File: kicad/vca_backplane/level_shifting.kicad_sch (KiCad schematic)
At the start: 8 parts, among them Q3 BSS138, Q4 BSS138, U2 74HCT245, U3 74LVC245

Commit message: v0.2 of backplane submitted to jlcpcb
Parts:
- added R24, R26, R27, R28, R29: 10k, Resistor_SMD:R_0603_1608Metric, symbol Device:R
- C2, C3: LCSC (none) -> C14663; LCSC Part C14663 -> (none)
- Q3, Q4: LCSC (none) -> C82045; LCSC Part C82045 -> (none)
- R1, R2: LCSC (none) -> C22978; LCSC Part C22978 -> (none)
- U2: LCSC (none) -> C5980; LCSC Part C5980 -> (none)
- U3: LCSC (none) -> C6082; LCSC Part C6082 -> (none)
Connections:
- net GND: now also R24.1, R26.1, R27.2, R28.1, R29.1
- net SPI_CLK_3V: now also U2.4 (A2)
- net SPI_MOSI_3V: now also U2.5 (A3)
- net SPI_MOSI2_5V: now reaches U2.15 (B3)
- net SPI_CLK2_5V: now reaches U2.16 (B2)
- net at U2.6 (A4): now also R24.2
- net at U2.7 (A5): now also R26.2
- net at U2.8 (A6): now also R29.2
- net at U2.9 (A7): now also R28.2
- net at U3.2 (A0): now also R27.1
- net SPI_CLK_5V renamed SPI_CLK1_5V
- net SPI_MOSI_5V renamed SPI_MOSI1_5V
- no-connect marks 14 -> 5
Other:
- note added: "SPI Level Shifting: Pi Out to Modules Clock and MOSI split for better fanout"
- note removed: "SPI Level Shifting: Pi Out to Modules"
- title: Level Shifting -> Zoxnoxious Backplane and VCA

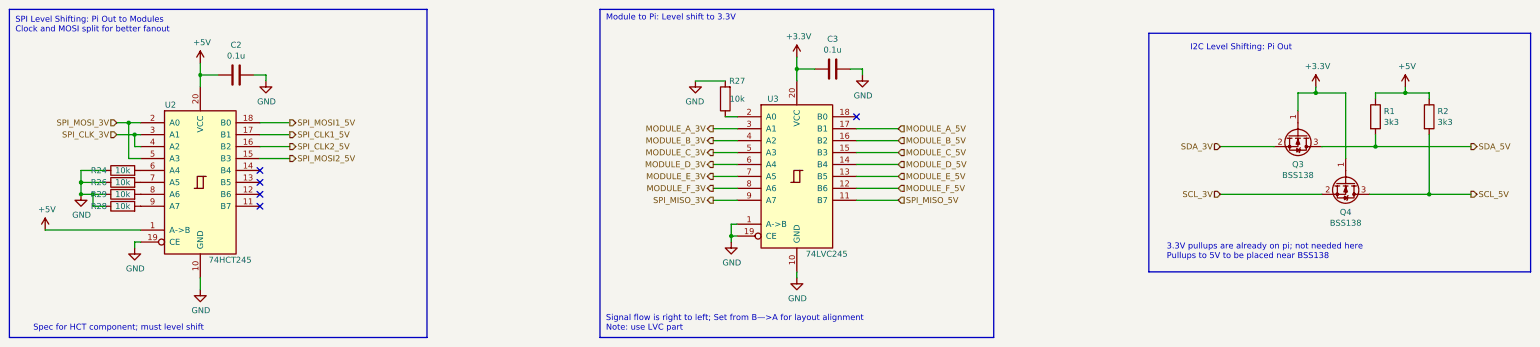
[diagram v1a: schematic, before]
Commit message: schematic for backplane v0.3: change Pi GPIOs for SPI; switch output jacks; add external input
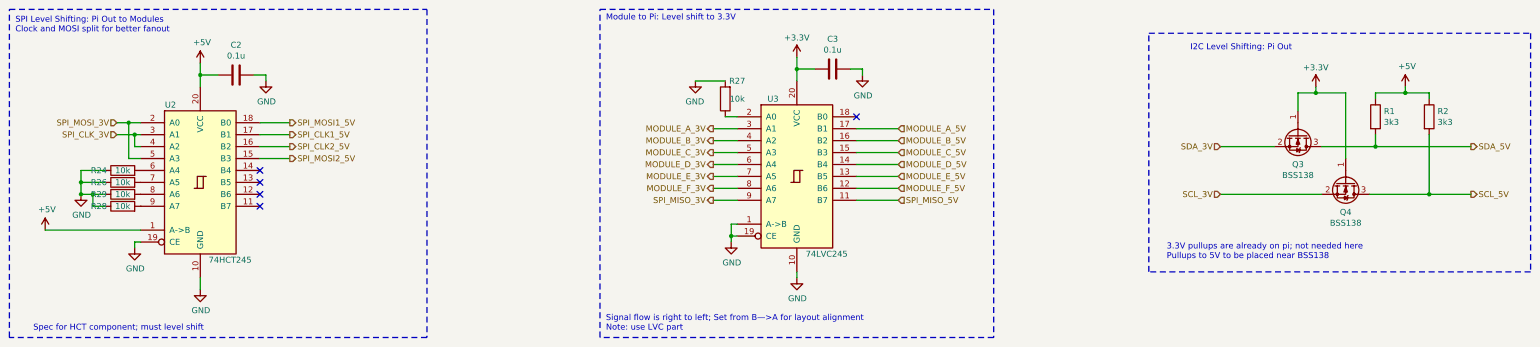
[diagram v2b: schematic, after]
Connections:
- net +3V3 renamed +3.3V

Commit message: working on placement
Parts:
- removed R26, R28, R29: 10k, Resistor_SMD:R_0603_1608Metric, symbol Device:R
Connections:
- net at R24.2, U2.6 (A4): now also U2.7 (A5), U2.8 (A6), U2.9 (A7)
- net at U3.18 (B0): now also R27.1
- net at U3.2 (A0): no longer R27.1
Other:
- moved on the sheet: R24, R27

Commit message: tightening up placement
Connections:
- net SPI_CLK1_5V: now also U2.18 (B0); no longer U2.17 (B1)
- net SPI_CLK_3V: now also U2.2 (A0); no longer U2.3 (A1)
- net SPI_MOSI1_5V: now also U2.17 (B1); no longer U2.18 (B0)
- net SPI_MOSI_3V: now also U2.3 (A1); no longer U2.2 (A0)
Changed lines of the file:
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@@
   (junction (at 331.47 81.28) (diameter 0) (color 0 0 0 0)
   )
+  (junction (at 54.61 68.58) (diameter 0) (color 0 0 0 0)
+  )
   (junction (at 326.39 59.69) (diameter 0) (color 0 0 0 0)
   )
@@
   (junction (at 182.88 90.17) (diameter 0) (color 0 0 0 0)
   )
-  (junction (at 54.61 66.04) (diameter 0) (color 0 0 0 0)
-  )
   (junction (at 69.85 55.88) (diameter 0) (color 0 0 0 0)
   )
@@
   (junction (at 307.34 59.69) (diameter 0) (color 0 0 0 0)
   )
-  (junction (at 55.88 68.58) (diameter 0) (color 0 0 0 0)
+  (junction (at 55.88 66.04) (diameter 0) (color 0 0 0 0)
   )
   (junction (at 196.85 54.61) (diameter 0) (color 0 0 0 0)
@@
     (stroke (width 0) (type dash))
   )
-  (wire (pts (xy 52.07 68.58) (xy 55.88 68.58))
-    (stroke (width 0) (type default))
-  )
   (polyline (pts (xy 29.21 41.91) (xy 118.11 41.91))
     (stroke (width 0) (type dash))
@@
     (stroke (width 0) (type default))
   )
+  (wire (pts (xy 55.88 66.04) (xy 57.15 66.04))
+    (stroke (width 0) (type default))
+  )
   (wire (pts (xy 215.9 63.5) (xy 215.9 64.77))
     (stroke (width 0) (type default))
@@
     (stroke (width 0) (type default))
   )
-  (wire (pts (xy 52.07 66.04) (xy 54.61 66.04))
-    (stroke (width 0) (type default))
-  )
   (polyline (pts (xy 154.94 41.91) (xy 238.76 41.91))
     (stroke (width 0) (type dash))
@@
     (stroke (width 0) (type default))
   )
-  (wire (pts (xy 55.88 68.58) (xy 55.88 71.12))
-    (stroke (width 0) (type default))
-  )
   (wire (pts (xy 184.15 80.01) (xy 179.07 80.01))
     (stroke (width 0) (type default))
@@
     (stroke (width 0) (type default))
   )
-  (wire (pts (xy 55.88 68.58) (xy 57.15 68.58))
+  (wire (pts (xy 52.07 68.58) (xy 54.61 68.58))
     (stroke (width 0) (type default))
   )
@@
     (stroke (width 0) (type default))
   )
+  (wire (pts (xy 55.88 66.04) (xy 55.88 71.12))
+    (stroke (width 0) (type default))
+  )
   (wire (pts (xy 209.55 69.85) (xy 218.44 69.85))
     (stroke (width 0) (type default))
@@
     (stroke (width 0) (type default))
   )
+  (wire (pts (xy 54.61 68.58) (xy 54.61 73.66))
+    (stroke (width 0) (type default))
+  )
   (wire (pts (xy 57.15 76.2) (xy 57.15 78.74))
     (stroke (width 0) (type default))
@@
     (stroke (width 0) (type default))
   )
-  (wire (pts (xy 54.61 66.04) (xy 57.15 66.04))
+  (wire (pts (xy 52.07 66.04) (xy 55.88 66.04))
     (stroke (width 0) (type default))
   )
@@
     (stroke (width 0) (type default))
   )
+  (wire (pts (xy 54.61 68.58) (xy 57.15 68.58))
+    (stroke (width 0) (type default))
+  )
   (wire (pts (xy 307.34 58.42) (xy 307.34 59.69))
     (stroke (width 0) (type default))
@@
   )
   (wire (pts (xy 209.55 64.77) (xy 215.9 64.77))
-    (stroke (width 0) (type default))
-  )
-  (wire (pts (xy 54.61 66.04) (xy 54.61 73.66))
     (stroke (width 0) (type default))
   )
@@
     (effects (font (size 1.27 1.27)) (justify left))
   )
-  (hierarchical_label "SPI_CLK_3V" (shape input) (at 52.07 68.58 180) (fields_autoplaced)
+  (hierarchical_label "SPI_CLK_3V" (shape input) (at 52.07 66.04 180) (fields_autoplaced)
     (effects (font (size 1.27 1.27)) (justify right))
   )
@@
     (effects (font (size 1.27 1.27)) (justify left))
   )
-  (hierarchical_label "SPI_MOSI1_5V" (shape output) (at 88.9 66.04 0) (fields_autoplaced)
-    (effects (font (size 1.27 1.27)) (justify left))
-  )
-  (hierarchical_label "SPI_MOSI_3V" (shape input) (at 52.07 66.04 180) (fields_autoplaced)
+  (hierarchical_label "SPI_MOSI1_5V" (shape output) (at 88.9 68.58 0) (fields_autoplaced)
+    (effects (font (size 1.27 1.27)) (justify left))
+  )
+  (hierarchical_label "SPI_MOSI_3V" (shape input) (at 52.07 68.58 180) (fields_autoplaced)
     (effects (font (size 1.27 1.27)) (justify right))
   )
@@
     (effects (font (size 1.27 1.27)) (justify right))
   )
-  (hierarchical_label "SPI_CLK1_5V" (shape output) (at 88.9 68.58 0) (fields_autoplaced)
-    (effects (font (size 1.27 1.27)) (justify left))
-  )
+  (hierarchical_label "SPI_CLK1_5V" (shape output) (at 88.9 66.04 0) (fields_autoplaced)
+    (effects (font (size 1.27 1.27)) (justify left))
+  )

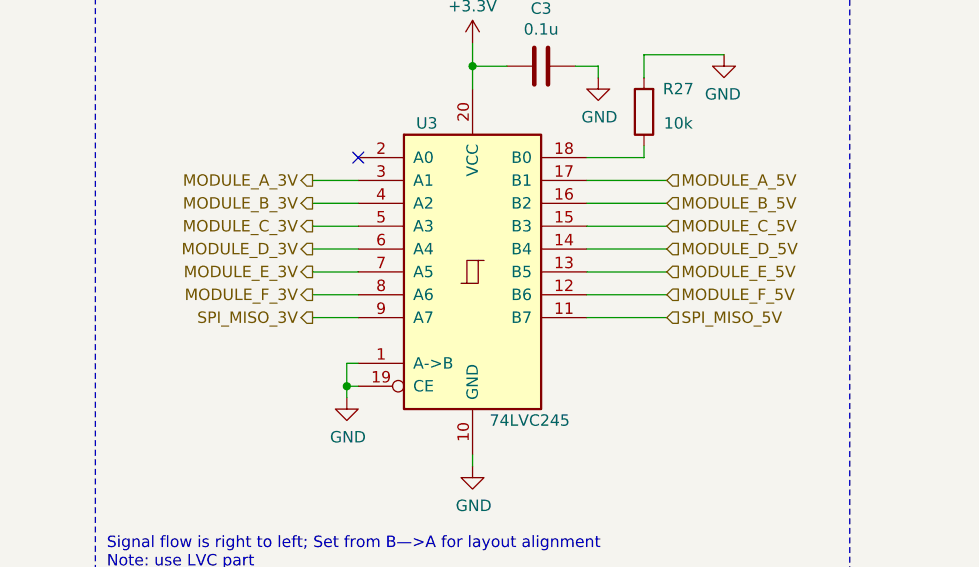
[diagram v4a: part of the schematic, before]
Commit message: add external input sheet.  Basic routing on backplane done- needs cleaning up
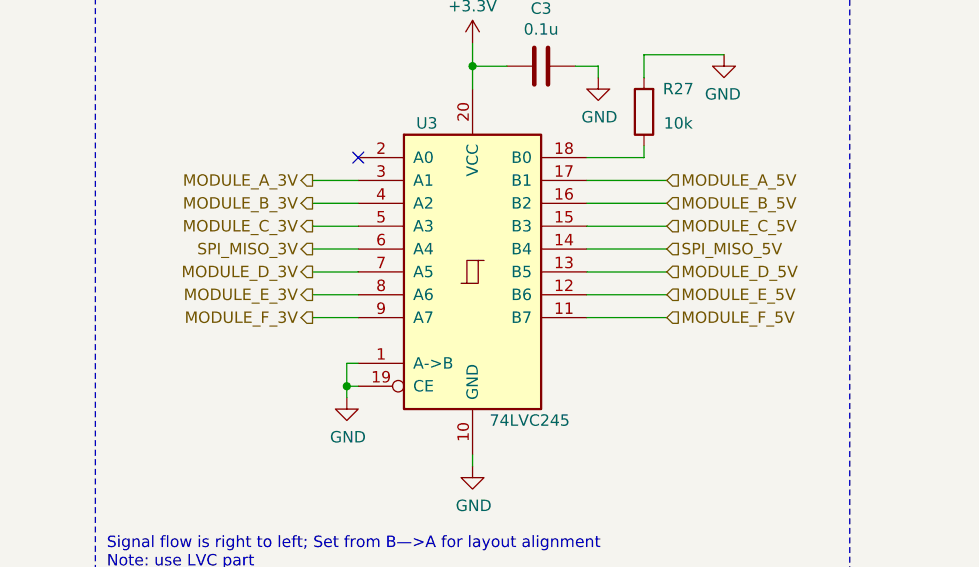
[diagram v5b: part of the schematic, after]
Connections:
- net MODULE_D_3V: now also U3.7 (A5); no longer U3.6 (A4)
- net MODULE_D_5V: now also U3.13 (B5); no longer U3.14 (B4)
- net MODULE_E_3V: now also U3.8 (A6); no longer U3.7 (A5)
- net MODULE_E_5V: now also U3.12 (B6); no longer U3.13 (B5)
- net MODULE_F_3V: now also U3.9 (A7); no longer U3.8 (A6)
- net MODULE_F_5V: now also U3.11 (B7); no longer U3.12 (B6)
- net SPI_MISO_3V: now also U3.6 (A4); no longer U3.9 (A7)
- net SPI_MISO_5V: now also U3.14 (B4); no longer U3.11 (B7)
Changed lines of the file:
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@@
     (effects (font (size 1.27 1.27)) (justify left bottom))
   )
-  (hierarchical_label "MODULE_F_3V" (shape output) (at 179.07 80.01 180) (fields_autoplaced)
+  (hierarchical_label "MODULE_F_3V" (shape output) (at 179.07 82.55 180) (fields_autoplaced)
     (effects (font (size 1.27 1.27)) (justify right))
   )
-  (hierarchical_label "MODULE_D_3V" (shape output) (at 179.07 74.93 180) (fields_autoplaced)
+  (hierarchical_label "MODULE_D_3V" (shape output) (at 179.07 77.47 180) (fields_autoplaced)
     (effects (font (size 1.27 1.27)) (justify right))
   )
@@
     (effects (font (size 1.27 1.27)) (justify right))
   )
-  (hierarchical_label "MODULE_F_5V" (shape input) (at 218.44 80.01 0) (fields_autoplaced)
+  (hierarchical_label "MODULE_F_5V" (shape input) (at 218.44 82.55 0) (fields_autoplaced)
     (effects (font (size 1.27 1.27)) (justify left))
   )
@@
     (effects (font (size 1.27 1.27)) (justify right))
   )
-  (hierarchical_label "MODULE_E_5V" (shape input) (at 218.44 77.47 0) (fields_autoplaced)
+  (hierarchical_label "MODULE_E_5V" (shape input) (at 218.44 80.01 0) (fields_autoplaced)
     (effects (font (size 1.27 1.27)) (justify left))
   )
@@
     (effects (font (size 1.27 1.27)) (justify right))
   )
-  (hierarchical_label "SPI_MISO_5V" (shape input) (at 218.44 82.55 0) (fields_autoplaced)
+  (hierarchical_label "SPI_MISO_5V" (shape input) (at 218.44 74.93 0) (fields_autoplaced)
     (effects (font (size 1.27 1.27)) (justify left))
   )
-  (hierarchical_label "MODULE_D_5V" (shape input) (at 218.44 74.93 0) (fields_autoplaced)
+  (hierarchical_label "MODULE_D_5V" (shape input) (at 218.44 77.47 0) (fields_autoplaced)
     (effects (font (size 1.27 1.27)) (justify left))
   )
-  (hierarchical_label "MODULE_E_3V" (shape output) (at 179.07 77.47 180) (fields_autoplaced)
+  (hierarchical_label "MODULE_E_3V" (shape output) (at 179.07 80.01 180) (fields_autoplaced)
     (effects (font (size 1.27 1.27)) (justify right))
   )
-  (hierarchical_label "SPI_MISO_3V" (shape output) (at 179.07 82.55 180) (fields_autoplaced)
+  (hierarchical_label "SPI_MISO_3V" (shape output) (at 179.07 74.93 180) (fields_autoplaced)
     (effects (font (size 1.27 1.27)) (justify right))
   )

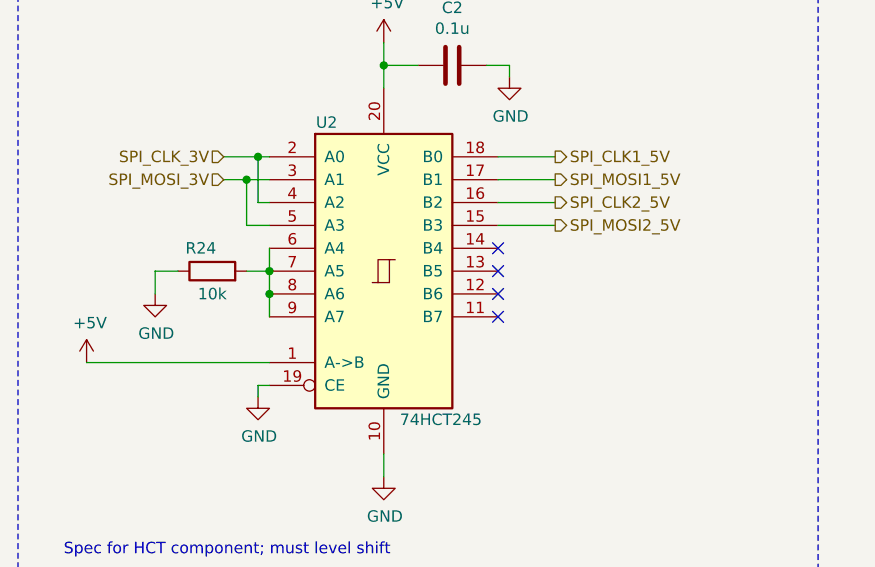
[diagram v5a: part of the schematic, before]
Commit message: use additional buffer for spi clock/mosi
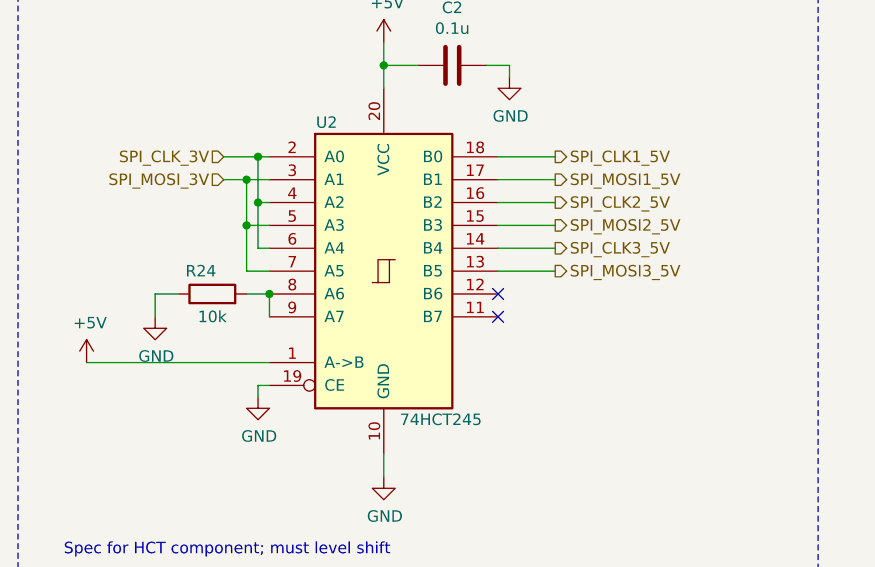
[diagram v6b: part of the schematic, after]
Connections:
- net SPI_CLK_3V: now also U2.6 (A4)
- net SPI_MOSI_3V: now also U2.7 (A5)
- net SPI_MOSI3_5V: now reaches U2.13 (B5)
- net SPI_CLK3_5V: now reaches U2.14 (B4)
- net at R24.2, U2.8 (A6), U2.9 (A7): no longer U2.6 (A4), U2.7 (A5)
- no-connect marks 5 -> 3
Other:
- moved on the sheet: R24
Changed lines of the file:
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@@
     (company "Zoxnoxious Engineering")
   )
+  (junction (at 55.88 71.12) (diameter 0) (color 0 0 0 0)
+  )
+  (junction (at 331.47 81.28) (diameter 0) (color 0 0 0 0)
+  )
+  (junction (at 54.61 68.58) (diameter 0) (color 0 0 0 0)
+  )
+  (junction (at 326.39 59.69) (diameter 0) (color 0 0 0 0)
+  )
+  (junction (at 320.04 71.12) (diameter 0) (color 0 0 0 0)
+  )
+  (junction (at 182.88 90.17) (diameter 0) (color 0 0 0 0)
+  )
+  (junction (at 54.61 73.66) (diameter 0) (color 0 0 0 0)
+  )
+  (junction (at 69.85 55.88) (diameter 0) (color 0 0 0 0)
+  )
   (junction (at 57.15 81.28) (diameter 0) (color 0 0 0 0)
   )
-  (junction (at 331.47 81.28) (diameter 0) (color 0 0 0 0)
-  )
-  (junction (at 54.61 68.58) (diameter 0) (color 0 0 0 0)
-  )
-  (junction (at 326.39 59.69) (diameter 0) (color 0 0 0 0)
-  )
-  (junction (at 320.04 71.12) (diameter 0) (color 0 0 0 0)
-  )
-  (junction (at 182.88 90.17) (diameter 0) (color 0 0 0 0)
-  )
-  (junction (at 69.85 55.88) (diameter 0) (color 0 0 0 0)
-  )
-  (junction (at 57.15 78.74) (diameter 0) (color 0 0 0 0)
-  )
   (junction (at 307.34 59.69) (diameter 0) (color 0 0 0 0)
   )
@@
   (junction (at 196.85 54.61) (diameter 0) (color 0 0 0 0)
   )
-  (no_connect (at 82.55 78.74))
-  (no_connect (at 82.55 76.2))
   (no_connect (at 82.55 83.82))
   (no_connect (at 184.15 64.77))
@@
     (stroke (width 0) (type default))
   )
-  (wire (pts (xy 57.15 78.74) (xy 57.15 81.28))
+  (wire (pts (xy 57.15 76.2) (xy 55.88 76.2))
     (stroke (width 0) (type default))
   )
@@
     (stroke (width 0) (type default))
   )
+  (wire (pts (xy 82.55 76.2) (xy 88.9 76.2))
+    (stroke (width 0) (type default))
+  )
   (wire (pts (xy 69.85 55.88) (xy 69.85 53.34))
     (stroke (width 0) (type default))
@@
     (stroke (width 0) (type default))
   )
-  (wire (pts (xy 44.45 81.28) (xy 44.45 78.74))
+  (wire (pts (xy 44.45 83.82) (xy 44.45 81.28))
     (stroke (width 0) (type default))
   )
@@
     (stroke (width 0) (type dash))
   )
+  (wire (pts (xy 57.15 78.74) (xy 54.61 78.74))
+    (stroke (width 0) (type default))
+  )
   (wire (pts (xy 69.85 99.06) (xy 69.85 101.6))
     (stroke (width 0) (type default))
@@
     (stroke (width 0) (type default))
   )
+  (wire (pts (xy 57.15 81.28) (xy 57.15 83.82))
+    (stroke (width 0) (type default))
+  )
   (wire (pts (xy 83.82 55.88) (xy 83.82 57.15))
     (stroke (width 0) (type default))
@@
     (stroke (width 0) (type default))
   )
-  (wire (pts (xy 57.15 76.2) (xy 57.15 78.74))
-    (stroke (width 0) (type default))
-  )
   (wire (pts (xy 208.28 54.61) (xy 210.82 54.61))
     (stroke (width 0) (type default))
@@
     (stroke (width 0) (type default))
   )
-  (wire (pts (xy 57.15 81.28) (xy 57.15 83.82))
-    (stroke (width 0) (type default))
-  )
   (wire (pts (xy 52.07 66.04) (xy 55.88 66.04))
     (stroke (width 0) (type default))
@@
     (stroke (width 0) (type dash))
   )
+  (wire (pts (xy 55.88 76.2) (xy 55.88 71.12))
+    (stroke (width 0) (type default))
+  )
   (wire (pts (xy 184.15 74.93) (xy 179.07 74.93))
     (stroke (width 0) (type default))
@@
     (stroke (width 0) (type default))
   )
-  (wire (pts (xy 54.61 78.74) (xy 57.15 78.74))
-    (stroke (width 0) (type default))
-  )
   (wire (pts (xy 196.85 54.61) (xy 196.85 52.07))
     (stroke (width 0) (type default))
@@
     (stroke (width 0) (type default))
   )
+  (wire (pts (xy 82.55 78.74) (xy 88.9 78.74))
+    (stroke (width 0) (type default))
+  )
   (wire (pts (xy 82.55 73.66) (xy 88.9 73.66))
     (stroke (width 0) (type default))
@@
     (stroke (width 0) (type default))
   )
+  (wire (pts (xy 54.61 81.28) (xy 57.15 81.28))
+    (stroke (width 0) (type default))
+  )
   (wire (pts (xy 313.69 73.66) (xy 313.69 59.69))
     (stroke (width 0) (type default))
@@
     (stroke (width 0) (type dash))
   )
+  (wire (pts (xy 54.61 78.74) (xy 54.61 73.66))
+    (stroke (width 0) (type default))
+  )
   (wire (pts (xy 82.55 71.12) (xy 88.9 71.12))
     (stroke (width 0) (type default))
@@
     (stroke (width 0) (type default))
   )
-  (wire (pts (xy 44.45 78.74) (xy 46.99 78.74))
+  (wire (pts (xy 44.45 81.28) (xy 46.99 81.28))
     (stroke (width 0) (type default))
   )
@@
     (effects (font (size 1.27 1.27)) (justify left))
   )
+  (hierarchical_label "SPI_MOSI3_5V" (shape output) (at 88.9 78.74 0) (fields_autoplaced)
+    (effects (font (size 1.27 1.27)) (justify left))
+  )
   (hierarchical_label "SPI_MOSI1_5V" (shape output) (at 88.9 68.58 0) (fields_autoplaced)
     (effects (font (size 1.27 1.27)) (justify left))
@@
   (hierarchical_label "MODULE_C_3V" (shape output) (at 179.07 72.39 180) (fields_autoplaced)
     (effects (font (size 1.27 1.27)) (justify right))
+  )
+  (hierarchical_label "SPI_CLK3_5V" (shape output) (at 88.9 76.2 0) (fields_autoplaced)
+    (effects (font (size 1.27 1.27)) (justify left))
   )
   (hierarchical_label "SDA_3V" (shape input) (at 287.02 71.12 180) (fields_autoplaced)
@@
     )
   )
-  (symbol (lib_id "Device:R") (at 50.8 78.74 90) (unit 1)
-    (in_bom yes) (on_board yes) (dnp no)
-    (property "Reference" "R24" (at 49.53 76.2 90)
-      (effects (font (size 1.27 1.27)))
-    )
-    (property "Value" "10k" (at 50.8 81.28 90)
-      (effects (font (size 1.27 1.27)))
-    )
-    (property "Footprint" "Resistor_SMD:R_0603_1608Metric" (at 50.8 80.518 90)
-      (effects (font (size 1.27 1.27)) hide)
-    )
-    (property "Datasheet" "~" (at 50.8 78.74 0)
-      (effects (font (size 1.27 1.27)) hide)
-    )
-    (property "LCSC" "C25804" (at 50.8 78.74 90)
+  (symbol (lib_id "Device:R") (at 50.8 81.28 90) (unit 1)
+    (in_bom yes) (on_board yes) (dnp no)
+    (property "Reference" "R24" (at 49.53 78.74 90)
+      (effects (font (size 1.27 1.27)))
+    )
+    (property "Value" "10k" (at 50.8 83.82 90)
+      (effects (font (size 1.27 1.27)))
+    )
+    (property "Footprint" "Resistor_SMD:R_0603_1608Metric" (at 50.8 83.058 90)
+      (effects (font (size 1.27 1.27)) hide)
+    )
+    (property "Datasheet" "~" (at 50.8 81.28 0)
+      (effects (font (size 1.27 1.27)) hide)
+    )
+    (property "LCSC" "C25804" (at 50.8 81.28 90)
       (effects (font (size 1.27 1.27)) hide)
     )
@@
     )
   )
-  (symbol (lib_id "power:GND") (at 44.45 81.28 0) (unit 1)
-    (in_bom yes) (on_board yes) (dnp no)
-    (property "Reference" "#PWR0173" (at 44.45 87.63 0)
-      (effects (font (size 1.27 1.27)) hide)
-    )
-    (property "Value" "GND" (at 44.577 85.6742 0)
-      (effects (font (size 1.27 1.27)))
-    )
-    (property "Footprint" "" (at 44.45 81.28 0)
-      (effects (font (size 1.27 1.27)) hide)
-    )
-    (property "Datasheet" "" (at 44.45 81.28 0)
-      (effects (font (size 1.27 1.27)) hide)
-    )
+  (symbol (lib_id "power:GND") (at 44.45 83.82 0) (unit 1)
+    (in_bom yes) (on_board yes) (dnp no)
+    (property "Reference" "#PWR0173" (at 44.45 90.17 0)
+      (effects (font (size 1.27 1.27)) hide)
+    )
+    (property "Value" "GND" (at 44.577 88.2142 0)
+      (effects (font (size 1.27 1.27)))
+    )
+    (property "Footprint" "" (at 44.45 83.82 0)
+      (effects (font (size 1.27 1.27)) hide)
+    )
+    (property "Datasheet" "" (at 44.45 83.82 0)
+      (effects (font (size 1.27 1.27)) hide)
+    )
